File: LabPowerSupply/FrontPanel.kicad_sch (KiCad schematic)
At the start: 27 parts, among them SW00 Decimal, SW01 0, SW02 Backspace, SW03 Current 2, SW04 Cancel, SW10 1, SW11 2, SW12 3, SW13 Voltage 2, SW14 Confirm, SW20 4, SW21 5, SW22 6, SW23 Current 1, SW24 Channel 2, SW30 7, SW31 8, SW32 7, SW33 Voltage 1, SW34 Channel 1

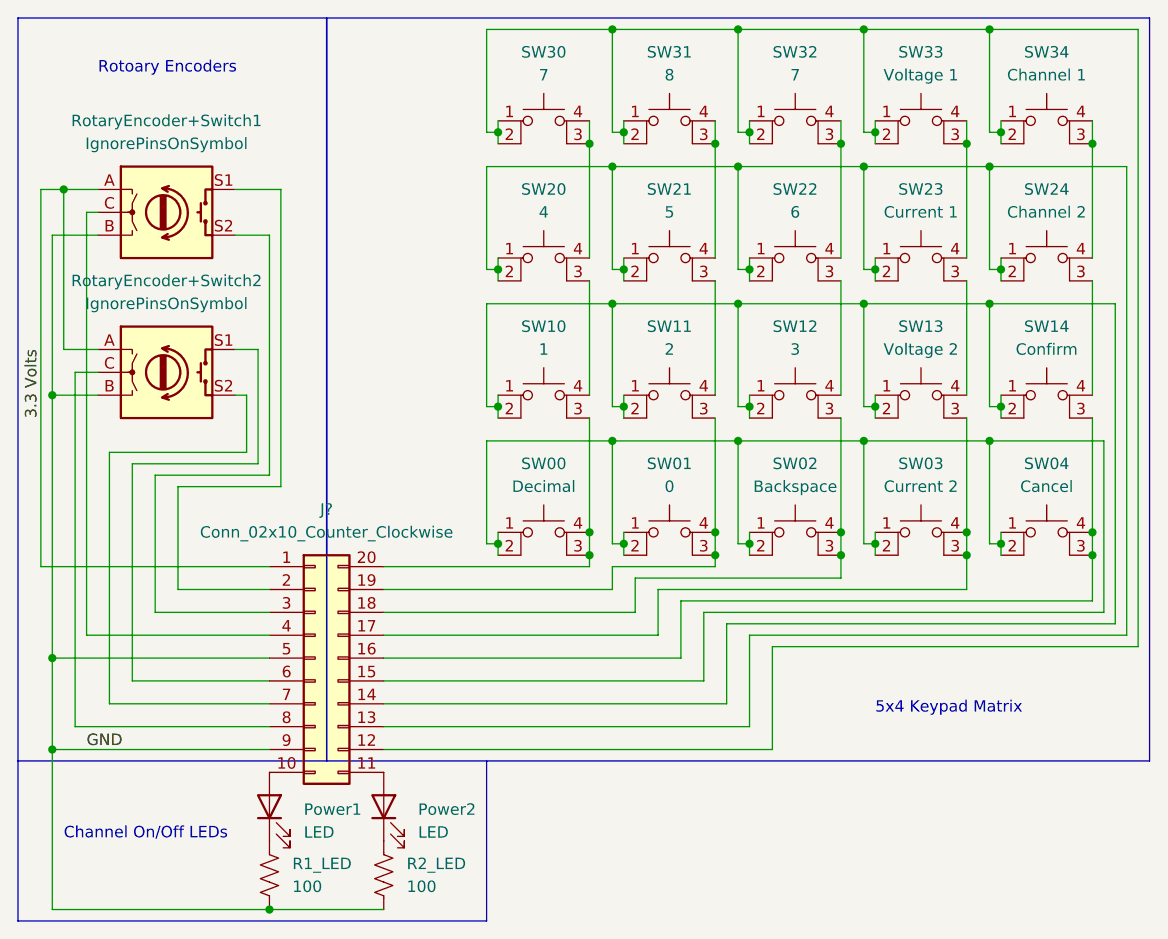
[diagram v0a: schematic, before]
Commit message: Finished first pass on the schematic
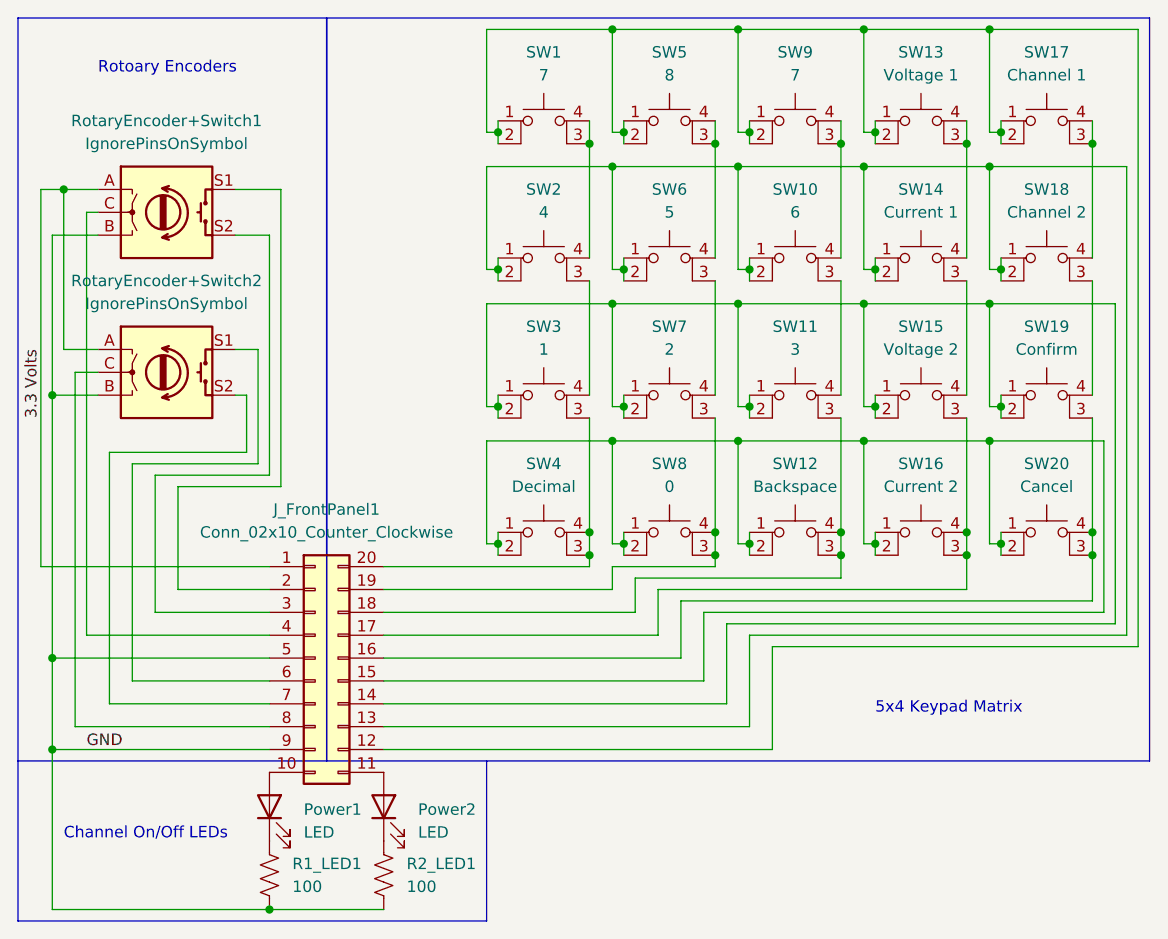
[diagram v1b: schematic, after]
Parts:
- gave numbers to parts that had none: 1
- renumbered R1_LED to R1_LED1, R2_LED to R2_LED1, SW30 to SW1, SW22 to SW10, SW12 to SW11, SW02 to SW12, SW33 to SW13, SW23 to SW14, SW13 to SW15, SW03 to SW16, SW34 to SW17, SW24 to SW18, SW14 to SW19, SW20 to SW2, SW04 to SW20, SW10 to SW3, SW00 to SW4, SW31 to SW5, SW21 to SW6, SW11 to SW7, SW01 to SW8, SW32 to SW9

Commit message: started PCB
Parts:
- RotaryEncoder+Switch1, RotaryEncoder+Switch2: footprint (none) -> Rotary_Encoder:RotaryEncoder_Alps_EC11E-Switch_Vertical_H20mm
- SW9: value 7 -> 9
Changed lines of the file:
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@@
     (rev "1")
     (company "George Mason University")
+    (comment 1 "MCU through a 2x10 JST plug.")
+    (comment 2 "this PCB as it has its own. The PCB will e connected to the primary")
+    (comment 3 "panel of thc case. The 20x04 Character LCD display is not part of")
+    (comment 4 "The front panel will be on a seperate PCB connected to the front")
   )
   (junction (at 179.07 97.79) (diameter 0) (color 0 0 0 0)
@@
     (property "Reference" "RotaryEncoder+Switch2" (id 0) (at 100.33 83.82 0))
     (property "Value" "IgnorePinsOnSymbol" (id 1) (at 100.33 86.36 0))
-    (property "Footprint" "" (id 2) (at 96.52 89.916 0)
+    (property "Footprint" "Rotary_Encoder:RotaryEncoder_Alps_EC11E-Switch_Vertical_H20mm" (id 2) (at 96.52 89.916 0)
       (effects (font (size 1.27 1.27)) hide)
     )
@@
     (in_bom yes) (on_board yes) (fields_autoplaced)
     (property "Reference" "SW9" (id 0) (at 170.18 58.42 0))
-    (property "Value" "7" (id 1) (at 170.18 60.96 0))
+    (property "Value" "9" (id 1) (at 170.18 60.96 0))
     (property "Footprint" "Button_Switch_SMD:SW_MEC_5GSH9" (id 2) (at 170.18 60.96 0)
       (effects (font (size 1.27 1.27)) hide)
@@
     (property "Reference" "RotaryEncoder+Switch1" (id 0) (at 100.33 66.04 0))
     (property "Value" "IgnorePinsOnSymbol" (id 1) (at 100.33 68.58 0))
-    (property "Footprint" "" (id 2) (at 96.52 72.136 0)
-      (effects (font (size 1.27 1.27)) hide)
-    )
+    (property "Footprint" "Rotary_Encoder:RotaryEncoder_Alps_EC11E-Switch_Vertical_H20mm" (id 2) (at 96.52 72.136 0)
+      (effects (font (size 1.27 1.27)) hide)
+    )

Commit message: more work
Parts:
- J_FrontPanel1: footprint Connector_JST:JST_PHD_B20B-PHDSS_2x10_P2.00mm_Vertical -> Connector_IDC:IDC-Header_2x10_P2.54mm_Vertical
- renumbered SW4 to SW11, SW8 to SW12, SW12 to SW13, SW16 to SW14, SW20 to SW15, SW3 to SW21, SW7 to SW22, SW11 to SW23, SW15 to SW24, SW19 to SW25, SW2 to SW31, SW6 to SW32, SW10 to SW33, SW14 to SW34, SW18 to SW35, SW1 to SW41, SW5 to SW42, SW9 to SW43, SW13 to SW44, SW17 to SW45
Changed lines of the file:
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@@
   (symbol (lib_id "Switch:SW_MEC_5E") (at 170.18 83.82 0) (unit 1)
     (in_bom yes) (on_board yes) (fields_autoplaced)
-    (property "Reference" "SW10" (id 0) (at 170.18 73.66 0))
+    (property "Reference" "SW33" (id 0) (at 170.18 73.66 0))
     (property "Value" "6" (id 1) (at 170.18 76.2 0))
     (property "Footprint" "Button_Switch_SMD:SW_MEC_5GSH9" (id 2) (at 170.18 76.2 0)
@@
   (symbol (lib_id "Switch:SW_MEC_5E") (at 156.21 114.3 0) (unit 1)
     (in_bom yes) (on_board yes) (fields_autoplaced)
-    (property "Reference" "SW8" (id 0) (at 156.21 104.14 0))
+    (property "Reference" "SW12" (id 0) (at 156.21 104.14 0))
     (property "Value" "0" (id 1) (at 156.21 106.68 0))
     (property "Footprint" "Button_Switch_SMD:SW_MEC_5GSH9" (id 2) (at 156.21 106.68 0)
@@
     (property "Reference" "J_FrontPanel1" (id 0) (at 118.11 109.22 0))
     (property "Value" "Conn_02x10_Counter_Clockwise" (id 1) (at 118.11 111.76 0))
-    (property "Footprint" "Connector_JST:JST_PHD_B20B-PHDSS_2x10_P2.00mm_Vertical" (id 2) (at 116.84 125.73 0)
+    (property "Footprint" "Connector_IDC:IDC-Header_2x10_P2.54mm_Vertical" (id 2) (at 116.84 125.73 0)
       (effects (font (size 1.27 1.27)) hide)
     )
@@
   (symbol (lib_id "Switch:SW_MEC_5E") (at 156.21 99.06 0) (unit 1)
     (in_bom yes) (on_board yes) (fields_autoplaced)
-    (property "Reference" "SW7" (id 0) (at 156.21 88.9 0))
+    (property "Reference" "SW22" (id 0) (at 156.21 88.9 0))
     (property "Value" "2" (id 1) (at 156.21 91.44 0))
     (property "Footprint" "Button_Switch_SMD:SW_MEC_5GSH9" (id 2) (at 156.21 91.44 0)
@@
   (symbol (lib_id "Switch:SW_MEC_5E") (at 142.24 99.06 0) (unit 1)
     (in_bom yes) (on_board yes) (fields_autoplaced)
-    (property "Reference" "SW3" (id 0) (at 142.24 88.9 0))
+    (property "Reference" "SW21" (id 0) (at 142.24 88.9 0))
     (property "Value" "1" (id 1) (at 142.24 91.44 0))
     (property "Footprint" "Button_Switch_SMD:SW_MEC_5GSH9" (id 2) (at 142.24 91.44 0)
@@
   (symbol (lib_id "Switch:SW_MEC_5E") (at 198.12 83.82 0) (unit 1)
     (in_bom yes) (on_board yes) (fields_autoplaced)
-    (property "Reference" "SW18" (id 0) (at 198.12 73.66 0))
+    (property "Reference" "SW35" (id 0) (at 198.12 73.66 0))
     (property "Value" "Channel 2" (id 1) (at 198.12 76.2 0))
     (property "Footprint" "Button_Switch_SMD:SW_MEC_5GSH9" (id 2) (at 198.12 76.2 0)
@@
   (symbol (lib_id "Switch:SW_MEC_5E") (at 198.12 68.58 0) (unit 1)
     (in_bom yes) (on_board yes) (fields_autoplaced)
-    (property "Reference" "SW17" (id 0) (at 198.12 58.42 0))
+    (property "Reference" "SW45" (id 0) (at 198.12 58.42 0))
     (property "Value" "Channel 1" (id 1) (at 198.12 60.96 0))
     (property "Footprint" "Button_Switch_SMD:SW_MEC_5GSH9" (id 2) (at 198.12 60.96 0)
@@
   (symbol (lib_id "Switch:SW_MEC_5E") (at 198.12 99.06 0) (unit 1)
     (in_bom yes) (on_board yes) (fields_autoplaced)
-    (property "Reference" "SW19" (id 0) (at 198.12 88.9 0))
+    (property "Reference" "SW25" (id 0) (at 198.12 88.9 0))
     (property "Value" "Confirm" (id 1) (at 198.12 91.44 0))
     (property "Footprint" "Button_Switch_SMD:SW_MEC_5GSH9" (id 2) (at 198.12 91.44 0)
@@
   (symbol (lib_id "Switch:SW_MEC_5E") (at 142.24 114.3 0) (unit 1)
     (in_bom yes) (on_board yes) (fields_autoplaced)
-    (property "Reference" "SW4" (id 0) (at 142.24 104.14 0))
+    (property "Reference" "SW11" (id 0) (at 142.24 104.14 0))
     (property "Value" "Decimal" (id 1) (at 142.24 106.68 0))
     (property "Footprint" "Button_Switch_SMD:SW_MEC_5GSH9" (id 2) (at 142.24 106.68 0)
@@
   (symbol (lib_id "Switch:SW_MEC_5E") (at 170.18 114.3 0) (unit 1)
     (in_bom yes) (on_board yes) (fields_autoplaced)
-    (property "Reference" "SW12" (id 0) (at 170.18 104.14 0))
+    (property "Reference" "SW13" (id 0) (at 170.18 104.14 0))
     (property "Value" "Backspace" (id 1) (at 170.18 106.68 0))
     (property "Footprint" "Button_Switch_SMD:SW_MEC_5GSH9" (id 2) (at 170.18 106.68 0)
@@
   (symbol (lib_id "Switch:SW_MEC_5E") (at 184.15 99.06 0) (unit 1)
     (in_bom yes) (on_board yes) (fields_autoplaced)
-    (property "Reference" "SW15" (id 0) (at 184.15 88.9 0))
+    (property "Reference" "SW24" (id 0) (at 184.15 88.9 0))
     (property "Value" "Voltage 2" (id 1) (at 184.15 91.44 0))
     (property "Footprint" "Button_Switch_SMD:SW_MEC_5GSH9" (id 2) (at 184.15 91.44 0)
@@
   (symbol (lib_id "Switch:SW_MEC_5E") (at 156.21 83.82 0) (unit 1)
     (in_bom yes) (on_board yes) (fields_autoplaced)
-    (property "Reference" "SW6" (id 0) (at 156.21 73.66 0))
+    (property "Reference" "SW32" (id 0) (at 156.21 73.66 0))
     (property "Value" "5" (id 1) (at 156.21 76.2 0))
     (property "Footprint" "Button_Switch_SMD:SW_MEC_5GSH9" (id 2) (at 156.21 76.2 0)
@@
   (symbol (lib_id "Switch:SW_MEC_5E") (at 170.18 68.58 0) (unit 1)
     (in_bom yes) (on_board yes) (fields_autoplaced)
-    (property "Reference" "SW9" (id 0) (at 170.18 58.42 0))
+    (property "Reference" "SW43" (id 0) (at 170.18 58.42 0))
     (property "Value" "9" (id 1) (at 170.18 60.96 0))
     (property "Footprint" "Button_Switch_SMD:SW_MEC_5GSH9" (id 2) (at 170.18 60.96 0)
@@
   (symbol (lib_id "Switch:SW_MEC_5E") (at 184.15 83.82 0) (unit 1)
     (in_bom yes) (on_board yes) (fields_autoplaced)
-    (property "Reference" "SW14" (id 0) (at 184.15 73.66 0))
+    (property "Reference" "SW34" (id 0) (at 184.15 73.66 0))
     (property "Value" "Current 1" (id 1) (at 184.15 76.2 0))
     (property "Footprint" "Button_Switch_SMD:SW_MEC_5GSH9" (id 2) (at 184.15 76.2 0)
@@
   (symbol (lib_id "Switch:SW_MEC_5E") (at 142.24 68.58 0) (unit 1)
     (in_bom yes) (on_board yes) (fields_autoplaced)
-    (property "Reference" "SW1" (id 0) (at 142.24 58.42 0))
+    (property "Reference" "SW41" (id 0) (at 142.24 58.42 0))
     (property "Value" "7" (id 1) (at 142.24 60.96 0))
     (property "Footprint" "Button_Switch_SMD:SW_MEC_5GSH9" (id 2) (at 142.24 60.96 0)
@@
   (symbol (lib_id "Switch:SW_MEC_5E") (at 156.21 68.58 0) (unit 1)
     (in_bom yes) (on_board yes) (fields_autoplaced)
-    (property "Reference" "SW5" (id 0) (at 156.21 58.42 0))
+    (property "Reference" "SW42" (id 0) (at 156.21 58.42 0))
     (property "Value" "8" (id 1) (at 156.21 60.96 0))
     (property "Footprint" "Button_Switch_SMD:SW_MEC_5GSH9" (id 2) (at 156.21 60.96 0)
@@
   (symbol (lib_id "Switch:SW_MEC_5E") (at 170.18 99.06 0) (unit 1)
     (in_bom yes) (on_board yes) (fields_autoplaced)
-    (property "Reference" "SW11" (id 0) (at 170.18 88.9 0))
+    (property "Reference" "SW23" (id 0) (at 170.18 88.9 0))
     (property "Value" "3" (id 1) (at 170.18 91.44 0))
     (property "Footprint" "Button_Switch_SMD:SW_MEC_5GSH9" (id 2) (at 170.18 91.44 0)
@@
   (symbol (lib_id "Switch:SW_MEC_5E") (at 184.15 68.58 0) (unit 1)
     (in_bom yes) (on_board yes) (fields_autoplaced)
-    (property "Reference" "SW13" (id 0) (at 184.15 58.42 0))
+    (property "Reference" "SW44" (id 0) (at 184.15 58.42 0))
     (property "Value" "Voltage 1" (id 1) (at 184.15 60.96 0))
     (property "Footprint" "Button_Switch_SMD:SW_MEC_5GSH9" (id 2) (at 184.15 60.96 0)
@@
   (symbol (lib_id "Switch:SW_MEC_5E") (at 198.12 114.3 0) (unit 1)
     (in_bom yes) (on_board yes) (fields_autoplaced)
-    (property "Reference" "SW20" (id 0) (at 198.12 104.14 0))
+    (property "Reference" "SW15" (id 0) (at 198.12 104.14 0))
     (property "Value" "Cancel" (id 1) (at 198.12 106.68 0))
     (property "Footprint" "Button_Switch_SMD:SW_MEC_5GSH9" (id 2) (at 198.12 106.68 0)
@@
   (symbol (lib_id "Switch:SW_MEC_5E") (at 142.24 83.82 0) (unit 1)
     (in_bom yes) (on_board yes) (fields_autoplaced)
-    (property "Reference" "SW2" (id 0) (at 142.24 73.66 0))
+    (property "Reference" "SW31" (id 0) (at 142.24 73.66 0))
     (property "Value" "4" (id 1) (at 142.24 76.2 0))
     (property "Footprint" "Button_Switch_SMD:SW_MEC_5GSH9" (id 2) (at 142.24 76.2 0)
@@
   (symbol (lib_id "Switch:SW_MEC_5E") (at 184.15 114.3 0) (unit 1)
     (in_bom yes) (on_board yes) (fields_autoplaced)
-    (property "Reference" "SW16" (id 0) (at 184.15 104.14 0))
+    (property "Reference" "SW14" (id 0) (at 184.15 104.14 0))
     (property "Value" "Current 2" (id 1) (at 184.15 106.68 0))
     (property "Footprint" "Button_Switch_SMD:SW_MEC_5GSH9" (id 2) (at 184.15 106.68 0)

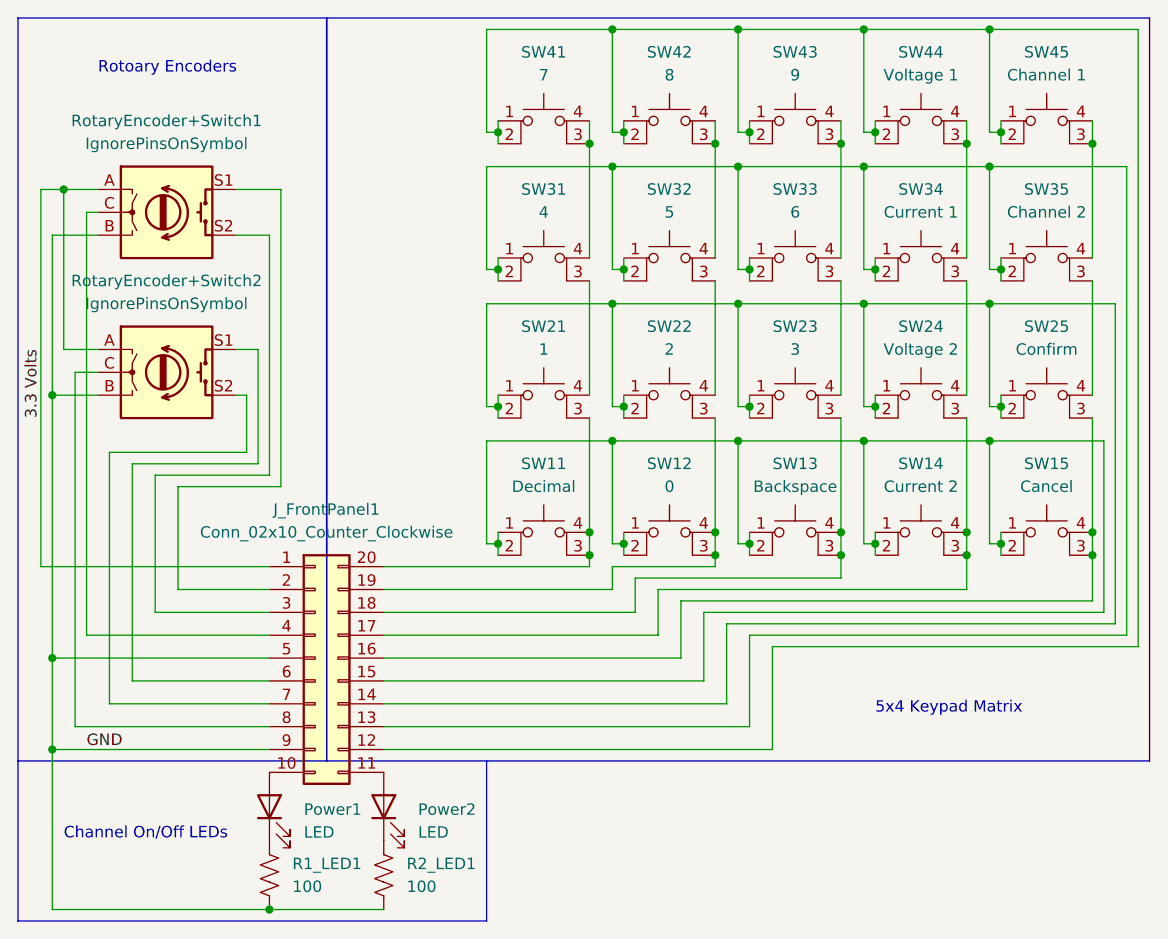
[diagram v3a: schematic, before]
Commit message: Resistor footprints changed to 0603
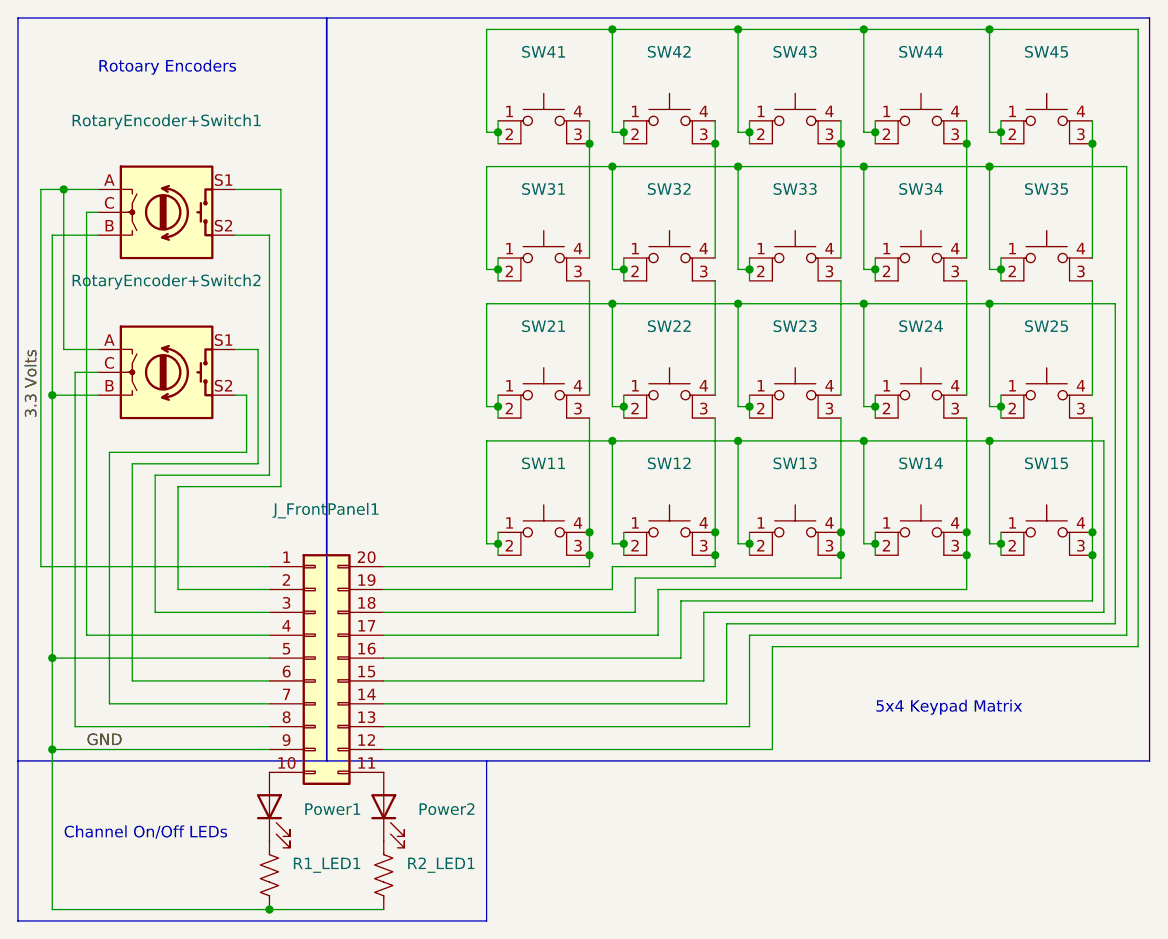
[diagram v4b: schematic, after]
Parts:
- J_FrontPanel1: value Conn_02x10_Counter_Clockwise -> (none); footprint Connector_IDC:IDC-Header_2x10_P2.54mm_Vertical -> (none)
- Power1, Power2: value LED -> (none); footprint LED_THT:LED_D3.0mm -> (none)
- R1_LED1, R2_LED1: value 100 -> (none); footprint Resistor_SMD:R_1210_3225Metric -> (none)
- RotaryEncoder+Switch1, RotaryEncoder+Switch2: value IgnorePinsOnSymbol -> (none); footprint Rotary_Encoder:RotaryEncoder_Alps_EC11E-Switch_Vertical_H20mm -> (none)
- SW11: value Decimal -> (none); footprint Button_Switch_SMD:SW_MEC_5GSH9 -> (none)
- SW12: value 0 -> (none); footprint Button_Switch_SMD:SW_MEC_5GSH9 -> (none)
- SW13: value Backspace -> (none); footprint Button_Switch_SMD:SW_MEC_5GSH9 -> (none)
- SW14: value Current 2 -> (none); footprint Button_Switch_SMD:SW_MEC_5GSH9 -> (none)
- SW15: value Cancel -> (none); footprint Button_Switch_SMD:SW_MEC_5GSH9 -> (none)
- SW21: value 1 -> (none); footprint Button_Switch_SMD:SW_MEC_5GSH9 -> (none)
- SW22: value 2 -> (none); footprint Button_Switch_SMD:SW_MEC_5GSH9 -> (none)
- SW23: value 3 -> (none); footprint Button_Switch_SMD:SW_MEC_5GSH9 -> (none)
- SW24: value Voltage 2 -> (none); footprint Button_Switch_SMD:SW_MEC_5GSH9 -> (none)
- SW25: value Confirm -> (none); footprint Button_Switch_SMD:SW_MEC_5GSH9 -> (none)
- SW31: value 4 -> (none); footprint Button_Switch_SMD:SW_MEC_5GSH9 -> (none)
- SW32: value 5 -> (none); footprint Button_Switch_SMD:SW_MEC_5GSH9 -> (none)
- SW33: value 6 -> (none); footprint Button_Switch_SMD:SW_MEC_5GSH9 -> (none)
- SW34: value Current 1 -> (none); footprint Button_Switch_SMD:SW_MEC_5GSH9 -> (none)
- SW35: value Channel 2 -> (none); footprint Button_Switch_SMD:SW_MEC_5GSH9 -> (none)
- SW41: value 7 -> (none); footprint Button_Switch_SMD:SW_MEC_5GSH9 -> (none)
- SW42: value 8 -> (none); footprint Button_Switch_SMD:SW_MEC_5GSH9 -> (none)
- SW43: value 9 -> (none); footprint Button_Switch_SMD:SW_MEC_5GSH9 -> (none)
- SW44: value Voltage 1 -> (none); footprint Button_Switch_SMD:SW_MEC_5GSH9 -> (none)
- SW45: value Channel 1 -> (none); footprint Button_Switch_SMD:SW_MEC_5GSH9 -> (none)
